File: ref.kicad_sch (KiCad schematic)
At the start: 25 parts, among them J61 Conn_01x01_Socket, J62 Conn_01x01_Socket, U6 REF7050, U61 OPA2189DGK

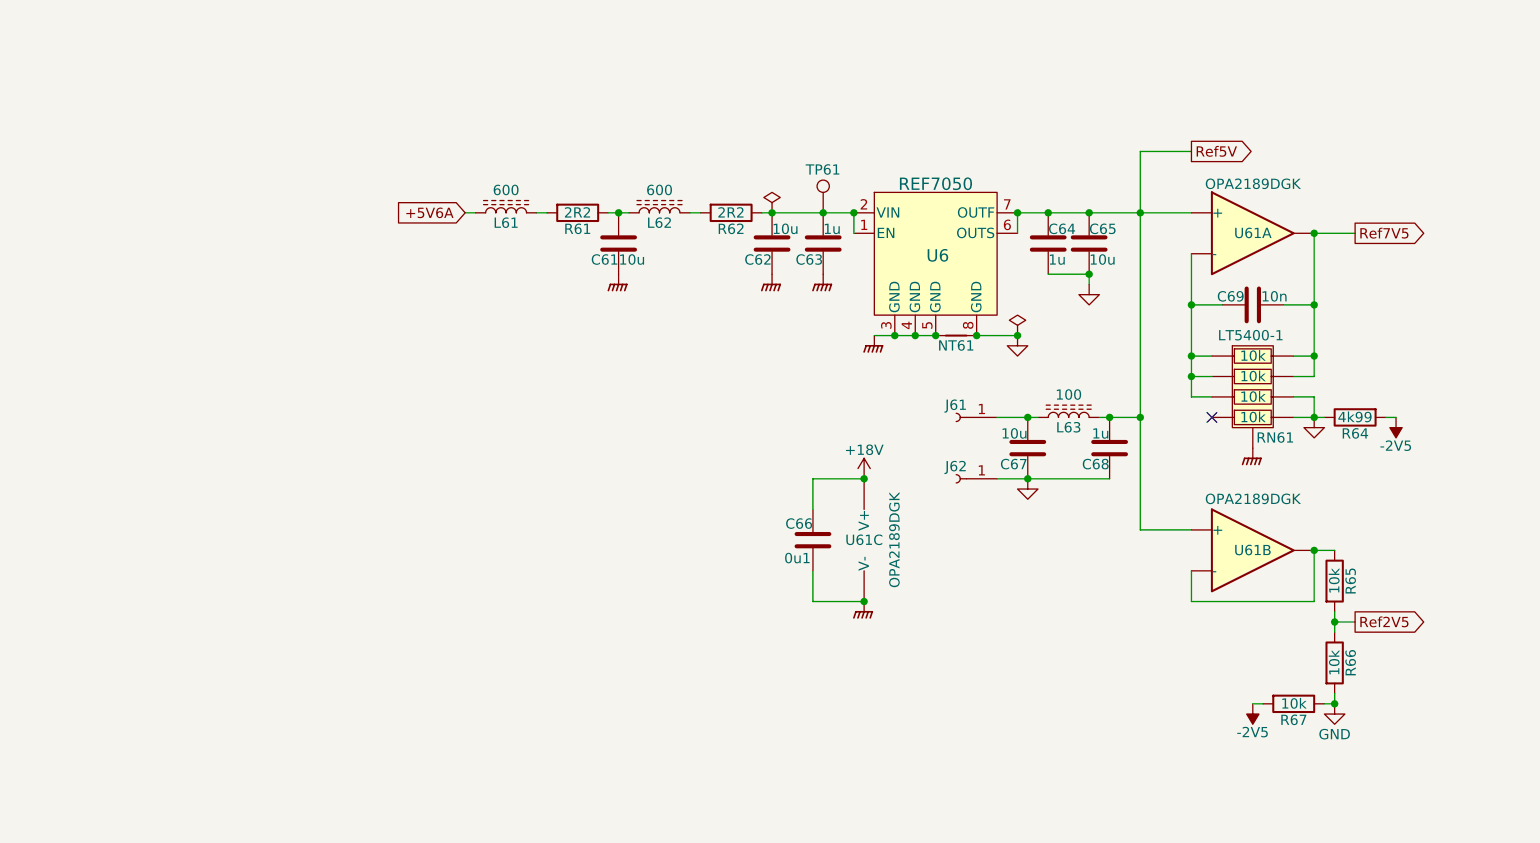
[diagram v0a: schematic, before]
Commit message: Tweaks following spice simulation.
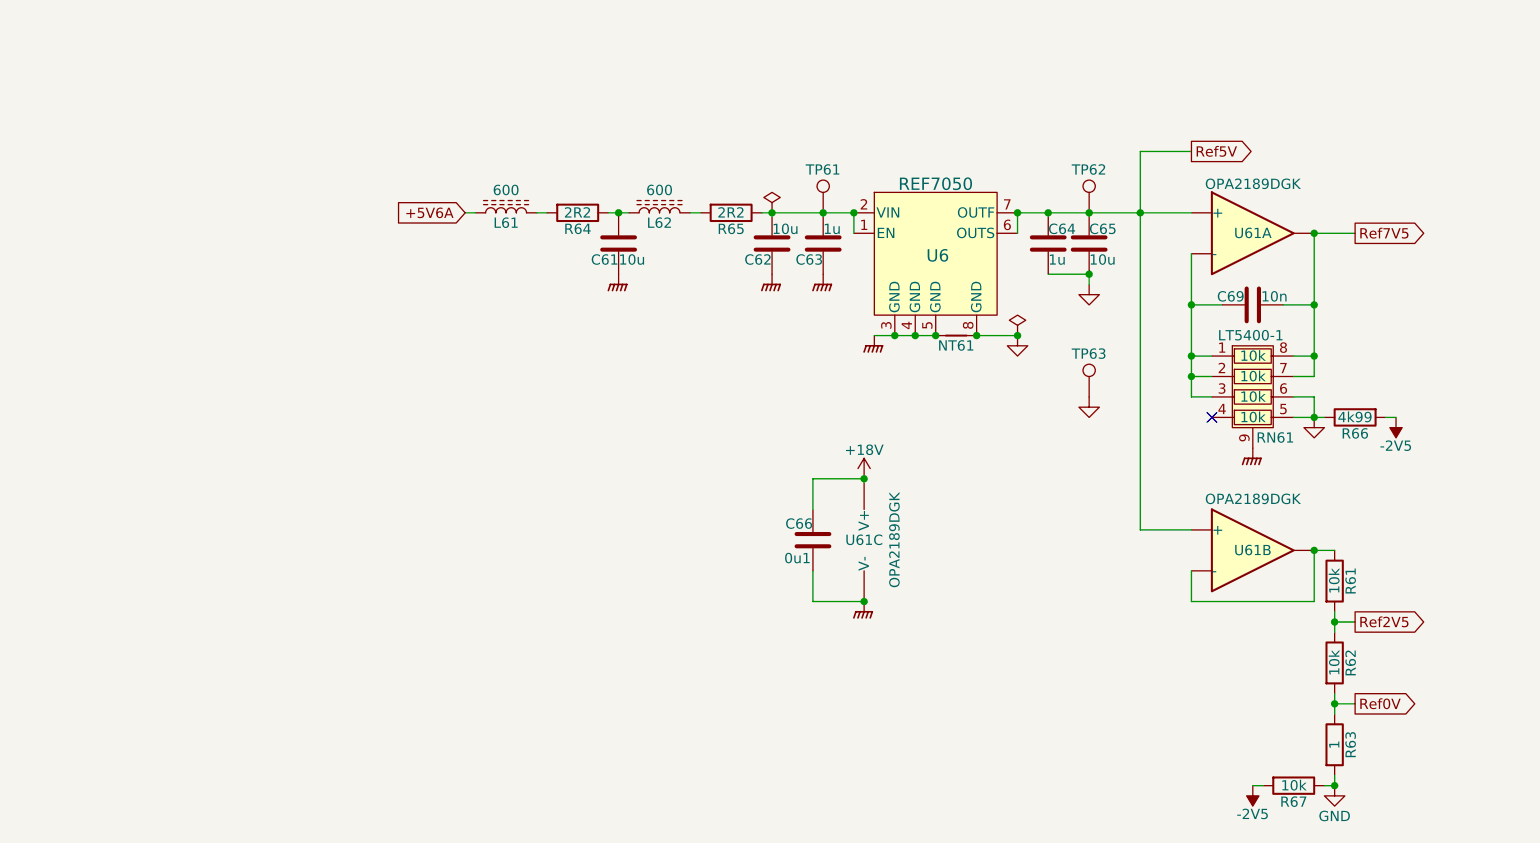
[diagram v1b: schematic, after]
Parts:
- removed C67: 10u, Capacitor_SMD:C_0603_1608Metric, symbol Device:C
- removed C68: 1u, Capacitor_SMD:C_0402_1005Metric, symbol Device:C
- removed J61, J62: Conn_01x01_Socket, TestPoint:TestPoint_Plated_Hole_D5.0mm, symbol Connector:Conn_01x01_Socket
- removed L63: 100, Inductor_SMD:L_0603_1608Metric, symbol Device:L_Ferrite
- added R63: 1, Resistor_SMD:R_0603_1608Metric, symbol Device:R
- added TP62, TP63: TestPoint, Parts:TestPoint, symbol Connector:TestPoint
- NT61: footprint NetTie:NetTie-2_SMD_Pad0.5mm -> Parts:NetTie-2_SMD_Pad0.5mm
- R61: renamed from R65; footprint Resistor_SMD:R_0402_1005Metric_Pad0.72x0.64mm_HandSolder -> Resistor_SMD:R_0603_1608Metric
- R62: renamed from R66; footprint Resistor_SMD:R_0402_1005Metric_Pad0.72x0.64mm_HandSolder -> Resistor_SMD:R_0603_1608Metric
- R67: footprint Resistor_SMD:R_0603_1608Metric -> Resistor_SMD:R_0402_1005Metric; LCSC C25804 -> C25744
- RN61: footprint Package_SO:MSOP-8-1EP_3x3mm_P0.65mm_EP1.68x1.88mm -> Parts:MSOP-8-1EP_3x3mm_P0.65mm_EP1.68x1.88mm
- renumbered R61 to R64, R62 to R65, R64 to R66
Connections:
- net GND: now also R63.2, TP63.1; no longer R62.2
- net Ref5V: now also TP62.1
- new net Ref0V: R62.2, R63.1
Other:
- moved on the sheet: R67

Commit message: About to delete scan...
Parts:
- added C68: 10n, Capacitor_SMD:C_0603_1608Metric, symbol Device:C
- added R68: 10, Resistor_SMD:R_0402_1005Metric, symbol Device:R
- C67: renamed from C69; value 10n -> 0n1; footprint Capacitor_SMD:C_0603_1608Metric -> Capacitor_SMD:C_0402_1005Metric; LCSC C307500 -> C1546
- TP61, TP62, TP63: Stock (none) -> -
- U61: Stock (none) -> 15
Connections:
- net GND: now also RN61.3, RN61.4, RN61.9, C68.2; no longer RN61.5, RN61.6
- net GNDPWR: no longer RN61.9
- net Ref7V5: now also RN61.1, RN61.2, C68.1, R68.2; no longer C67.1, RN61.7, RN61.8, U61.1
- new net: C67.1, R68.1, U61.1
- new net: C67.2, RN61.6, RN61.7, RN61.8, U61.2 (-)
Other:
- note added: "≈250µV"
- moved on the sheet: C67

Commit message: Most blocks there....
About to restore scan.
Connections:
- net rin: now reaches C62.1, C63.1, R65.1, TP61.1, U6.1 (EN), U6.2 (VIN)
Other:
- moved on the sheet: C66, U61C
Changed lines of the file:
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@@
 	)
 	(junction
-		(at 134.62 116.84)
+		(at 162.56 118.11)
 		(diameter 0)
 		(color 0 0 0 0)
@@
 	)
 	(junction
-		(at 134.62 101.6)
+		(at 162.56 102.87)
 		(diameter 0)
 		(color 0 0 0 0)
@@
 	(wire
 		(pts
-			(xy 128.27 101.6) (xy 134.62 101.6)
+			(xy 156.21 102.87) (xy 162.56 102.87)
 		)
 		(stroke
@@
 	(wire
 		(pts
-			(xy 128.27 116.84) (xy 134.62 116.84)
+			(xy 156.21 118.11) (xy 162.56 118.11)
 		)
 		(stroke
@@
 	(wire
 		(pts
-			(xy 128.27 113.03) (xy 128.27 116.84)
+			(xy 156.21 114.3) (xy 156.21 118.11)
 		)
 		(stroke
@@
 	(wire
 		(pts
-			(xy 128.27 101.6) (xy 128.27 105.41)
+			(xy 156.21 102.87) (xy 156.21 106.68)
 		)
 		(stroke
@@
 		)
 	)
+	(label "rin"
+		(at 125.73 68.58 0)
+		(effects
+			(font
+				(size 1.27 1.27)
+			)
+			(justify left bottom)
+		)
+	)
 	(global_label "+5V6A"
 		(shape input)
@@
 	(symbol
 		(lib_id "Parts:OPA2189DGK")
-		(at 134.62 109.22 0)
+		(at 162.56 110.49 0)
 		(unit 3)
 		(exclude_from_sim no)
@@
 		(dnp no)
 		(property "Reference" "U61"
-			(at 134.62 109.22 0)
+			(at 162.56 110.49 0)
 			(effects
 				(font
@@
 		)
 		(property "Value" "OPA2189DGK"
-			(at 138.43 109.22 90)
+			(at 166.37 110.49 90)
 			(effects
 				(font
@@
 		)
 		(property "Footprint" "Parts:OPA2189"
-			(at 133.35 109.22 0)
+			(at 161.29 110.49 0)
 			(effects
 				(font
@@
 		)
 		(property "Datasheet" "http://www.ti.com/lit/ds/symlink/opa189.pdf"
-			(at 133.35 109.22 0)
+			(at 161.29 110.49 0)
 			(effects
 				(font
@@
 		)
 		(property "Description" ""
-			(at 133.35 109.22 0)
+			(at 161.29 110.49 0)
 			(effects
 				(font
@@
 		)
 		(property "LCSC" "C881489"
-			(at 134.62 109.22 0)
+			(at 162.56 110.49 0)
 			(effects
 				(font
@@
 		)
 		(property "Stock" "15"
-			(at 134.62 109.22 0)
+			(at 162.56 110.49 0)
 			(effects
 				(font
@@
 	(symbol
 		(lib_id "power:GNDPWR")
-		(at 134.62 116.84 0)
+		(at 162.56 118.11 0)
 		(unit 1)
 		(exclude_from_sim no)
@@
 		(dnp no)
 		(property "Reference" "#PWR0306"
-			(at 134.62 123.19 0)
+			(at 162.56 124.46 0)
 			(effects
 				(font
@@
 		)
 		(property "Value" "GNDPWR"
-			(at 134.62 120.142 0)
+			(at 162.56 121.412 0)
 			(effects
 				(font
@@
 		)
 		(property "Footprint" ""
-			(at 134.62 118.11 0)
+			(at 162.56 119.38 0)
 			(effects
 				(font
@@
 		)
 		(property "Datasheet" ""
-			(at 134.62 118.11 0)
+			(at 162.56 119.38 0)
 			(effects
 				(font
@@
 		)
 		(property "Description" "Power symbol creates a global label with name \"GNDPWR\" , global ground"
-			(at 134.62 116.84 0)
+			(at 162.56 118.11 0)
 			(effects
 				(font
@@
 	(symbol
 		(lib_id "Parts:+18V")
-		(at 134.62 101.6 0)
+		(at 162.56 102.87 0)
 		(unit 1)
 		(exclude_from_sim no)
@@
 		(dnp no)
 		(property "Reference" "#PWR0307"
-			(at 134.62 105.41 0)
+			(at 162.56 106.68 0)
 			(effects
 				(font
@@
 		)
 		(property "Value" "+18V"
-			(at 134.62 98.044 0)
+			(at 162.56 99.314 0)
 			(do_not_autoplace yes)
 			(effects
@@
 		)
 		(property "Footprint" ""
-			(at 134.62 101.6 0)
+			(at 162.56 102.87 0)
 			(effects
 				(font
@@
 		)
 		(property "Datasheet" ""
-			(at 134.62 101.6 0)
+			(at 162.56 102.87 0)
 			(effects
 				(font
@@
 		)
 		(property "Description" "Power symbol creates a global label with name {dblquote}+18V{dblquote}"
-			(at 134.62 101.6 0)
+			(at 162.56 102.87 0)
 			(effects
 				(font
@@
 	(symbol
 		(lib_id "Device:C")
-		(at 128.27 109.22 0)
+		(at 156.21 110.49 0)
 		(mirror y)
 		(unit 1)
@@
 		(dnp no)
 		(property "Reference" "C66"
-			(at 128.27 107.95 0)
+			(at 156.21 109.22 0)
 			(effects
 				(font
@@
 		)
 		(property "Value" "0u1"
-			(at 128.016 110.744 0)
+			(at 155.956 112.014 0)
 			(effects
 				(font
@@
 		)
 		(property "Footprint" "Capacitor_SMD:C_0402_1005Metric"
-			(at 127.3048 113.03 0)
+			(at 155.2448 114.3 0)
 			(effects
 				(font
@@
 		)
 		(property "Datasheet" "X7R, 50V"
-			(at 128.27 109.22 0)
+			(at 156.21 110.49 0)
 			(effects
 				(font
@@
 		)
 		(property "Description" "Unpolarized capacitor"
-			(at 128.27 109.22 0)
+			(at 156.21 110.49 0)
 			(effects
 				(font
@@
 		)
 		(property "LCSC" "C307331"
-			(at 128.27 109.22 0)
+			(at 156.21 110.49 0)
 			(effects
 				(font
@@
 		)
 		(property "Stock" ""
-			(at 128.27 109.22 0)
+			(at 156.21 110.49 0)
 			(effects
 				(font
@@
 		(dnp no)
 		(property "Reference" "R65"
-			(at 118.11 70.612 90)
+			(at 118.11 66.548 90)
 			(effects
 				(font
@@
 		(dnp no)
 		(property "Reference" "R64"
-			(at 99.06 70.612 90)
+			(at 99.06 66.548 90)
 			(effects
 				(font

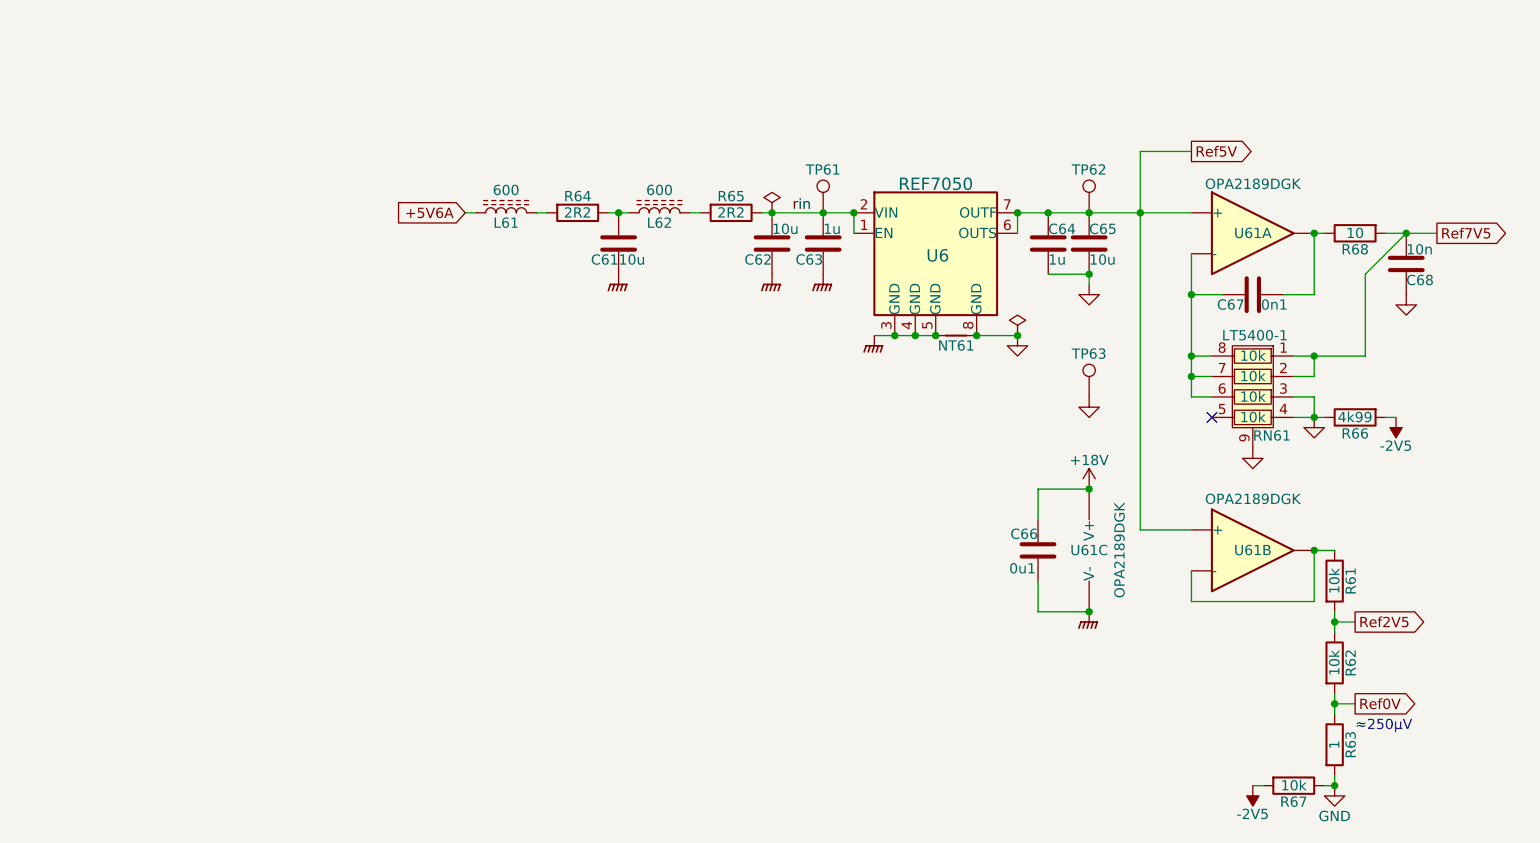
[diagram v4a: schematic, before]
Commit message: Put ref filtering into the schematic.
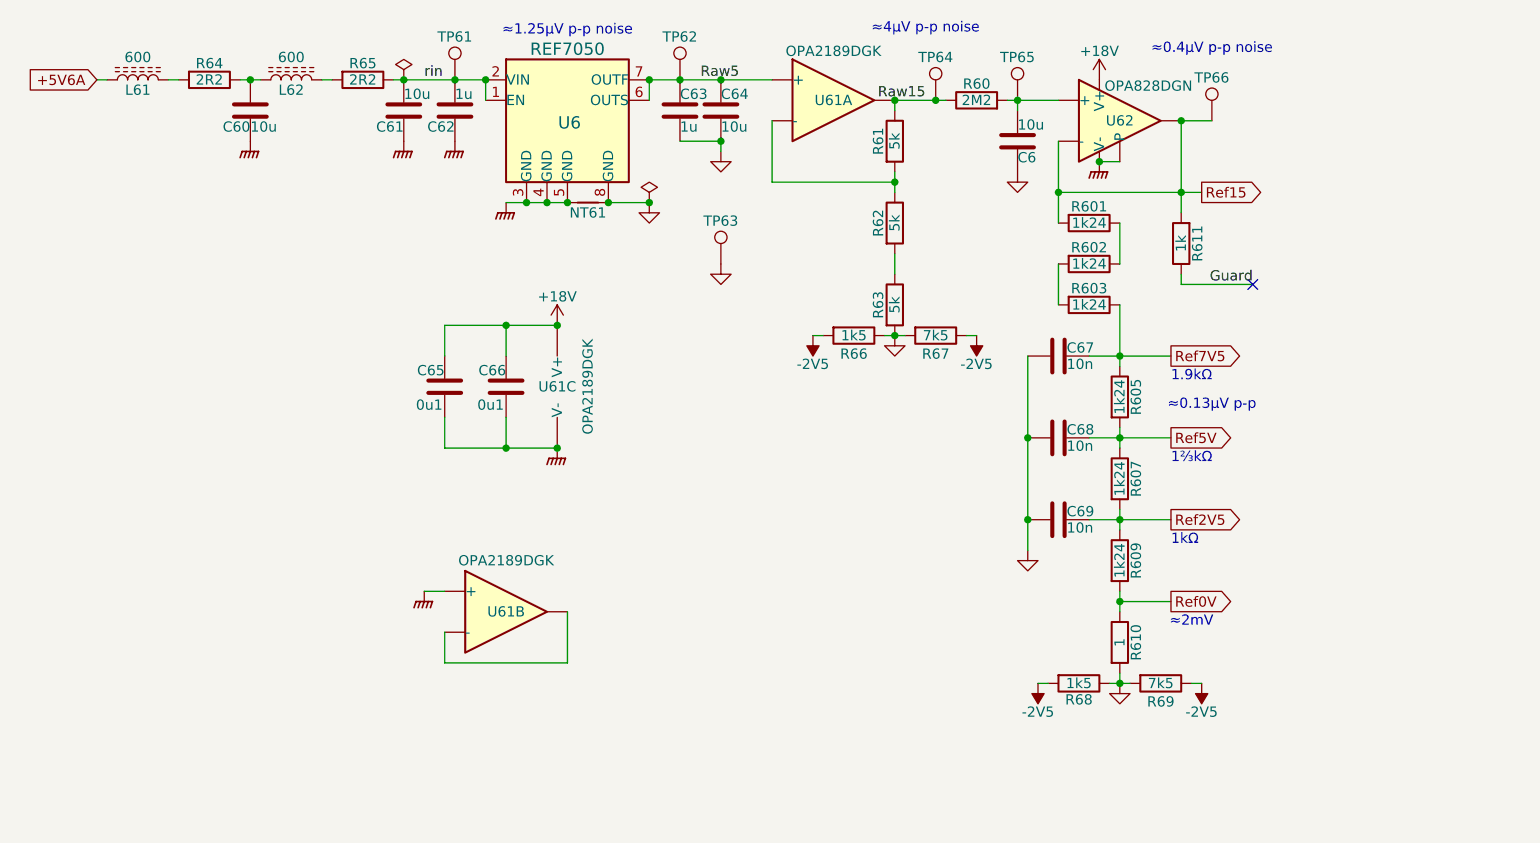
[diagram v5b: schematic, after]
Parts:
- removed RN61: LT5400-1, Parts:MSOP-8-1EP_3x3mm_P0.65mm_EP1.68x1.88mm, symbol Parts:LT5400
- added C6: 10u, Parts:C_Rect_L31.5mm_W15.0mm_P27.50mm_MKS4, symbol Device:C
- added C65: 0u1, Capacitor_SMD:C_0402_1005Metric, symbol Device:C
- added C69: 10n, Capacitor_SMD:C_0603_1608Metric, symbol Device:C
- added R60: 2M2, Resistor_SMD:R_0603_1608Metric, symbol Device:R
- added R601, R602, R603, R605, R607, R609: 1k24, Resistor_SMD:R_1206_3216Metric, symbol Device:R
- added R610: 1, Resistor_SMD:R_0603_1608Metric, symbol Device:R
- added R611: 1k, Resistor_SMD:R_0603_1608Metric, symbol Device:R
- added R69: 7k5, Resistor_SMD:R_0603_1608Metric, symbol Device:R
- added TP64, TP65, TP66: TestPoint, Parts:TestPoint, symbol Connector:TestPoint
- added U62: OPA828DGN, Parts:VSSOP-8-1EP_3x3mm_P0.65mm_EP1.57x1.89mm, symbol Parts:OPA828DGN
- C67: value 0n1 -> 10n; footprint Capacitor_SMD:C_0402_1005Metric -> Capacitor_SMD:C_0603_1608Metric; LCSC C1546 -> C307500
- R61, R62: value 10k -> 5k; footprint Resistor_SMD:R_0603_1608Metric -> Resistor_SMD:R_1206_3216Metric
- R63: value 1 -> 5k; footprint Resistor_SMD:R_0603_1608Metric -> Resistor_SMD:R_1206_3216Metric
- R66: value 4k99 -> 1k5; footprint Resistor_SMD:R_0603_1608Metric -> Resistor_SMD:R_0402_1005Metric; LCSC C23046 -> C25867
- R67: value 10k -> 7k5; footprint Resistor_SMD:R_0402_1005Metric -> Resistor_SMD:R_0603_1608Metric; LCSC C25744 -> C23234
- R68: value 10 -> 1k5; LCSC C25077 -> C25867
- renumbered C61 to C60, C62 to C61, C63 to C62, C64 to C63, C65 to C64
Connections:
- net +18V: now also C65.1, U62.7 (V+)
- net -2V5: now also R67.1, R68.2, R69.1; no longer R67.2
- net GND: now also C67.2, R67.2, R68.1, C6.2, C69.2, R610.2, R69.2; no longer R67.1
- net GNDPWR: now also U61.5 (+), C65.2, U62.4 (V-), U62.9 (P)
- net Ref0V: now also R609.2, R610.1; no longer R62.2, R63.1
- net Ref2V5: now also C69.1, R607.2, R609.1; no longer R61.2, R62.1
- net Ref5V: now also C68.1, R605.2, R607.1; no longer C63.1, C64.1, TP62.1, U6.6 (OUTS), U6.7 (OUTF), U61.3 (+), U61.5 (+)
- net Ref7V5: now also C67.1, R603.1, R605.1; no longer C68.1, R68.2
- net at U61.2 (-): now also R61.2, R62.1; no longer C67.2
- net at U61.6 (-), U61.7: no longer R61.1
- new net: C6.1, R60.2, TP65.1, U62.3 (+)
- new net: R601.1, R602.1
- new net: R602.2, R603.2
- new net: R62.2, R63.1
- new net Guard: R611.1
- new net Raw15: R60.1, R61.1, TP64.1, U61.1
- new net Raw5: C63.1, C64.1, TP62.1, U6.6 (OUTS), U6.7 (OUTF), U61.3 (+)
- new net Ref15: R601.2, R611.2, TP66.1, U62.2 (-), U62.6
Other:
- note added: "1.9kΩ"
- note added: "1kΩ"
- note added: "1⅔kΩ"
- note added: "≈0.13µV p-p"
- note added: "≈0.4µV p-p noise"
- note added: "≈1.25µV p-p noise"
- note added: "≈2mV"
- note added: "≈4µV p-p noise"
- note removed: "≈250µV"
- moved on the sheet: C60, C61, C62, C63, C64, C66, L61, L62, NT61, R64, R65, TP61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
